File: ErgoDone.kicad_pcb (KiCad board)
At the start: 2 copper layers, 182.8 x 158.9 mm, 151 parts, among them J1 USB, J2 3.5mm, J3 JMP, J4 JMP, SW0:10 SW0:3, SW0:11 SW0:2, SW0:12 SW0:1, SW0:7 SW0:6, SW0:8 SW0:5, SW0:9 SW0:4, SW1:10 SW1:3, SW1:11 SW1:2, SW1:12 SW1:1, SW1:13 SW1:0, SW1:9 SW1:4, SW2:10 SW2:3, SW2:11 SW2:2, SW2:12 SW2:1, SW2:13 SW2:0, SW2:7 SW2:6, SW2:8 SW2:5, SW2:9 SW2:4, SW3:10 SW3:3, SW3:11 SW3:2, SW3:12 SW3:1, SW3:13 SW3:0, SW3:8 SW3:5, SW3:9 SW3:4, SW4:10 SW4:3, SW4:11 SW4:2, SW4:12 SW4:1, SW4:13 SW4:0, SW4:7 SW4:6, SW4:8 SW4:5, SW4:9 SW4:4, SW5:10 SW5:3, SW5:11 SW5:2, SW5:12 SW5:1, SW5:13 SW5:0, SW5:7 SW5:6, SW5:8 SW5:5, SW5:9 SW5:4, U1 ProMicro, U2 MCP23017

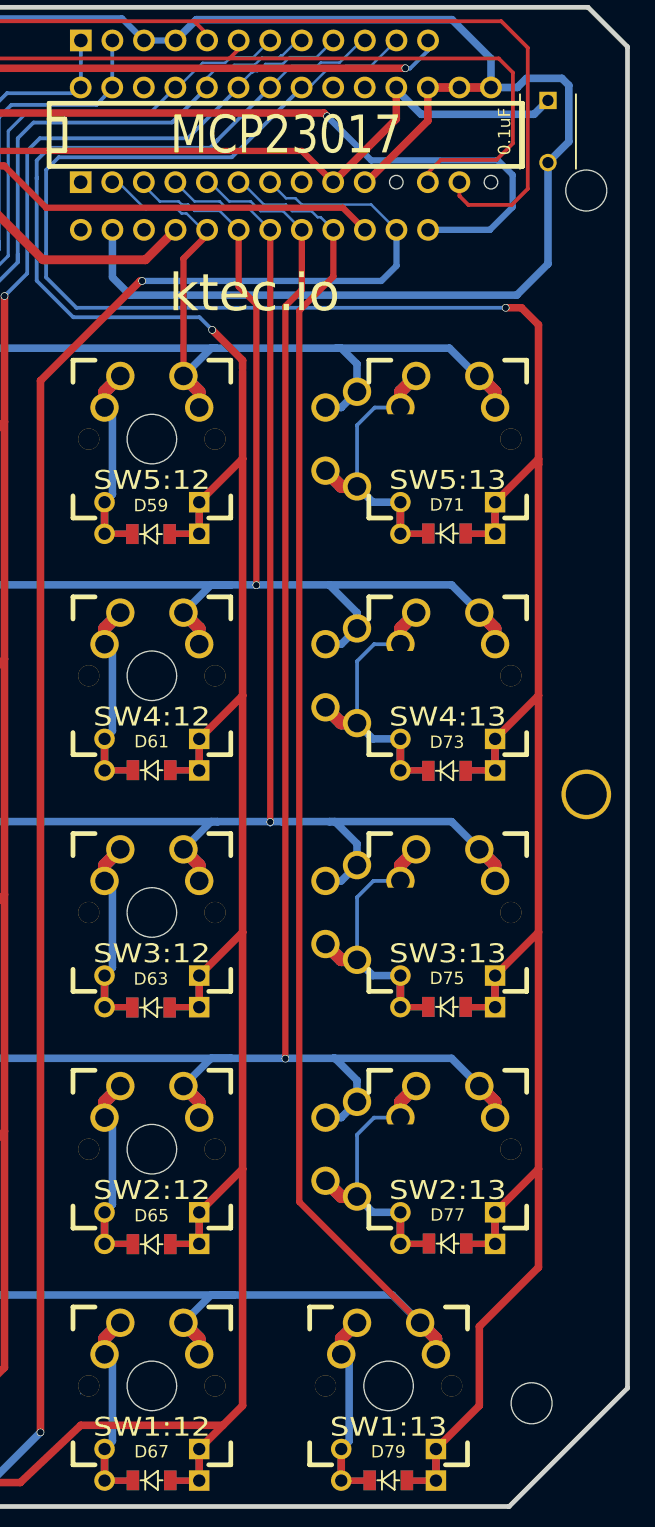
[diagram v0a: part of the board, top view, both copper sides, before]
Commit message: Changed outer column to 1u and moved capacitor to make more room on the outside edge.
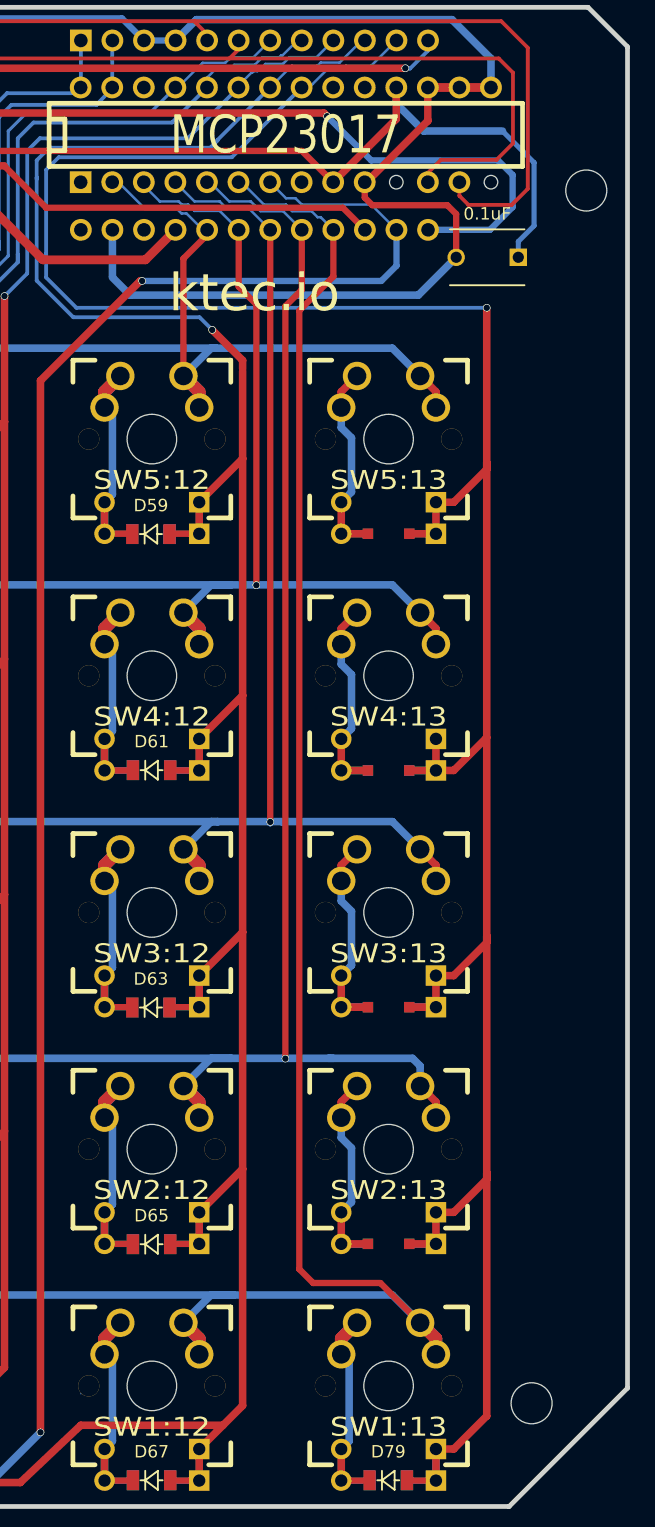
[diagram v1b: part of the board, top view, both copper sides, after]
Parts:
- removed D71, D73, D75, D77: DIODE, ErgoDone:D_1206_L
- removed D72, D74, D76, D78: DIODE, ErgoDone:D_1206_R
- removed the REF** at (202.6, 95.6)
- SW2:13, SW3:13, SW4:13, SW5:13: footprint ErgoDone:MX_FLIP_XX_NOSMD -> ErgoDone:MX_FLIP_DIODE
- moved C1 12.8 mm to (197.1, 52.4), turned to 180 degrees
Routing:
- net /COL0: track 246.3 -> 215.4 mm
- net Net-(D71-Pad1): track 35.8 -> 13.9 mm
- net Net-(D77-Pad1): track 35.9 -> 14.2 mm
- net Net-(D75-Pad1): track 35.4 -> 13.9 mm
- net Net-(D73-Pad1): track 34.1 -> 13.9 mm
- net GND: track 243.0 -> 226.5 mm
- net /ROW4: track 241.6 -> 226.3 mm
- net /ROW5: track 211.8 -> 196.5 mm
- net /ROW3: track 220.3 -> 205.6 mm
- net /ROW2: track 277.7 -> 263.8 mm
- net VCC: track 168.7 -> 177.8 mm
- net /ROW1: track 306.2 -> 309.3 mm
- net (no net): track 3.80 -> 3.20 mm
- net /LED_B: track 145.2 -> 145.8 mm

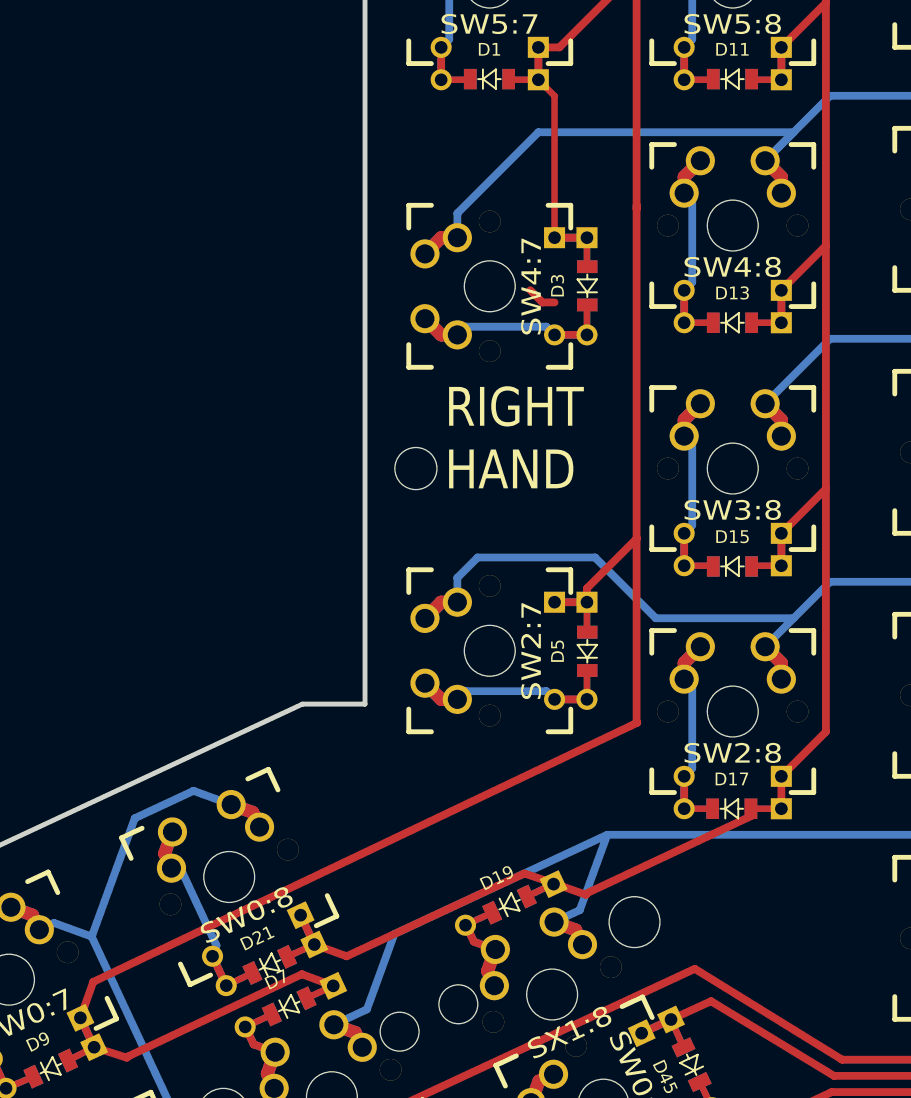
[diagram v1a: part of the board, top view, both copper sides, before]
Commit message: Innwards column pads rotate and add one more switch
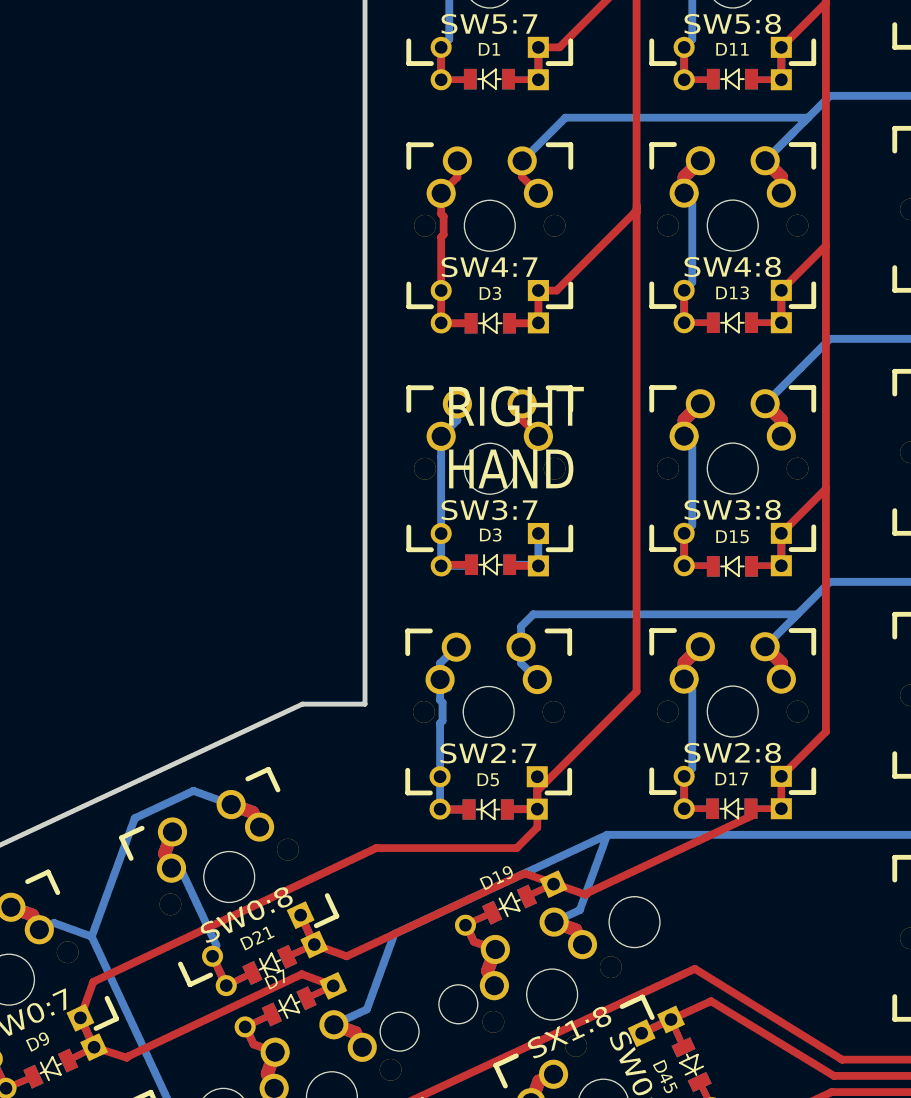
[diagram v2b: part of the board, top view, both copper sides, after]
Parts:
- removed the REF** at (66.6, 102.9)
- added D3: DIODE, ErgoDone:D_1206_L, F.Cu at (72.5, 110.7)
- added D4: DIODE, ErgoDone:D_1206_R, B.Cu at (72.5, 110.7)
- added SW3:7: SW3:6, ErgoDone:MX_FLIP_DIODE_NOSMD, F.Cu at (72.4, 103.2)
- moved D5 14.6 mm to (72.3, 129.9), turned to 0 degrees
- moved D6 14.6 mm to (72.3, 129.9), turned to 0 degrees
- moved D3 8.15 mm to (72.4, 91.8), turned to 0 degrees
- moved D4 8.15 mm to (72.4, 91.8), turned to 0 degrees
- moved SW2:7 4.80 mm to (72.3, 122.3), turned to 0 degrees
- moved SW4:7 4.75 mm to (72.4, 84.2), turned to 0 degrees
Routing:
- net (no net): track 3.20 -> 29.2 mm
- net /COL6: track 305.4 -> 292.9 mm
- net /ROW2: track 263.8 -> 253.5 mm
- net /ROW4: track 226.3 -> 216.5 mm
- net Net-(D3-Pad1): track 24.1 -> 18.1 mm
- net Net-(D5-Pad1): track 23.9 -> 18.9 mm

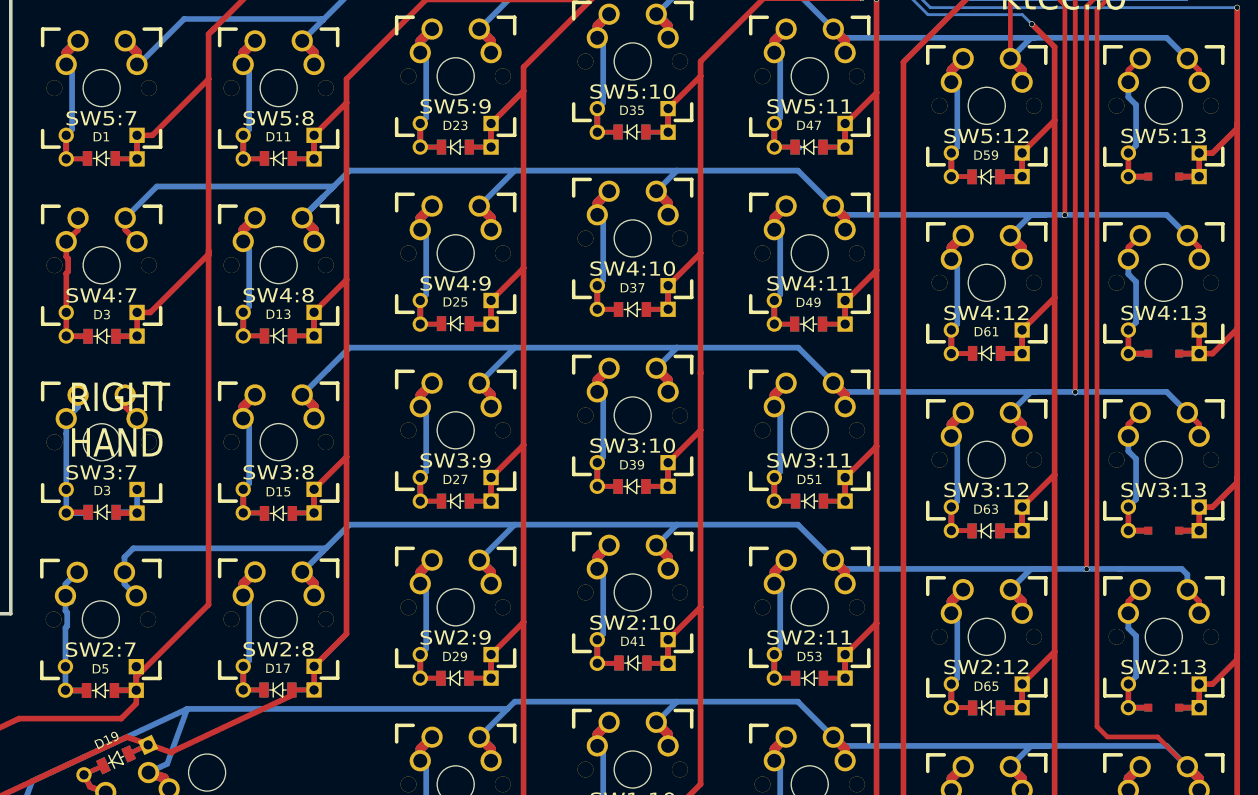
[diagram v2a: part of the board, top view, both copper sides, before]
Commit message: Updating net and placing missing diodes.
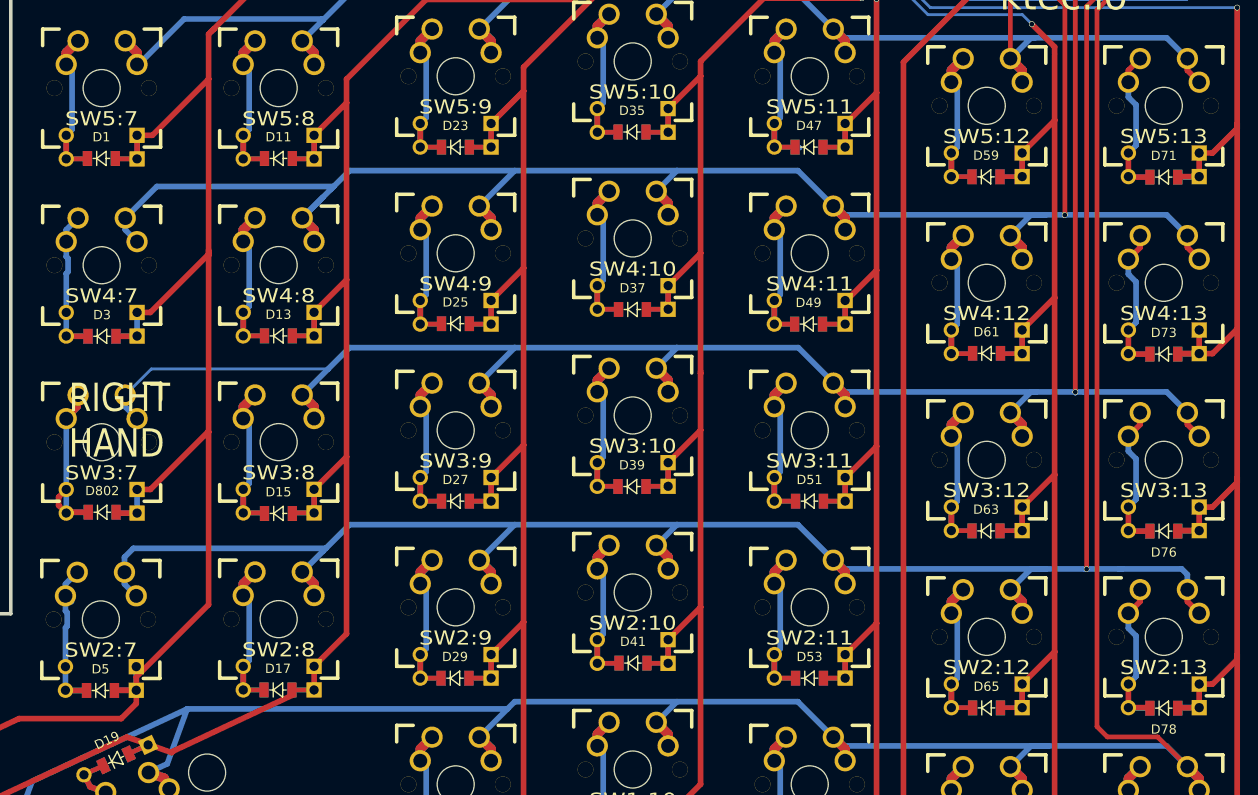
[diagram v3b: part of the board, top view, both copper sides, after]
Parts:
- removed the D3 at (72.5, 110.7)
- removed the D4 at (72.5, 110.7)
- added D71: DIODE, ErgoDone:D_1206_L, F.Cu at (186.7, 74.7)
- added D72: DIODE, ErgoDone:D_1206_R, B.Cu at (186.7, 74.7)
- added D73: DIODE, ErgoDone:D_1206_L, F.Cu at (186.7, 93.7)
- added D74: DIODE, ErgoDone:D_1206_R, B.Cu at (186.7, 93.7)
- added D75: DIODE, ErgoDone:D_1206_L, B.Cu at (186.7, 112.8)
- added D76: DIODE, ErgoDone:D_1206_R, F.Cu at (186.7, 112.8)
- added D77: DIODE, ErgoDone:D_1206_L, B.Cu at (186.7, 131.8)
- added D78: DIODE, ErgoDone:D_1206_R, F.Cu at (186.7, 131.8)
- added D801: DIODE, ErgoDone:D_1206_R, B.Cu at (72.5, 110.7)
- added D802: DIODE, ErgoDone:D_1206_L, F.Cu at (72.5, 110.7)
- SW2:13, SW3:13, SW4:13, SW5:13: footprint ErgoDone:MX_FLIP_DIODE -> ErgoDone:MX_FLIP_DIODE_NOSMD
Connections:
- SW3:7 pad 1: (no net) -> /ROW3
- SW3:7 pad 2: (no net) -> Net-(D801-Pad1)
- SW3:7 pad 3: (no net) -> Net-(D801-Pad1)
- SW3:7 pad 4: (no net) -> /COL6
- U1 pad 27: (no net) -> Net-(U1-Pad27)
- U1 pad 29: (no net) -> Net-(U1-Pad29)
- U2 pad 1: (no net) -> Net-(U2-Pad1)
- U2 pad 19: (no net) -> Net-(U2-Pad19)
- U2 pad 20: (no net) -> Net-(U2-Pad20)
- U2 pad 26: (no net) -> Net-(U2-Pad26)
- U2 pad 8: (no net) -> Net-(U2-Pad8)
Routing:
- net (no net): track 29.2 -> 0.90 mm
- net /ROW3: track 205.6 -> 231.6 mm
- net Net-(D801-Pad1): track 0.00 -> 23.4 mm
- net /COL0: track 215.4 -> 234.0 mm
- net /COL6: track 292.9 -> 310.4 mm
- net Net-(D73-Pad1): track 13.9 -> 18.6 mm
- net Net-(D75-Pad1): track 13.9 -> 18.6 mm
- net Net-(D77-Pad1): track 14.2 -> 18.9 mm
- net Net-(D71-Pad1): track 13.9 -> 18.6 mm
